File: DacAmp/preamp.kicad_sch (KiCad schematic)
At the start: 34 parts, among them U3 NE5532, U6 NE5532, U7 NE5532, U8 NE5532

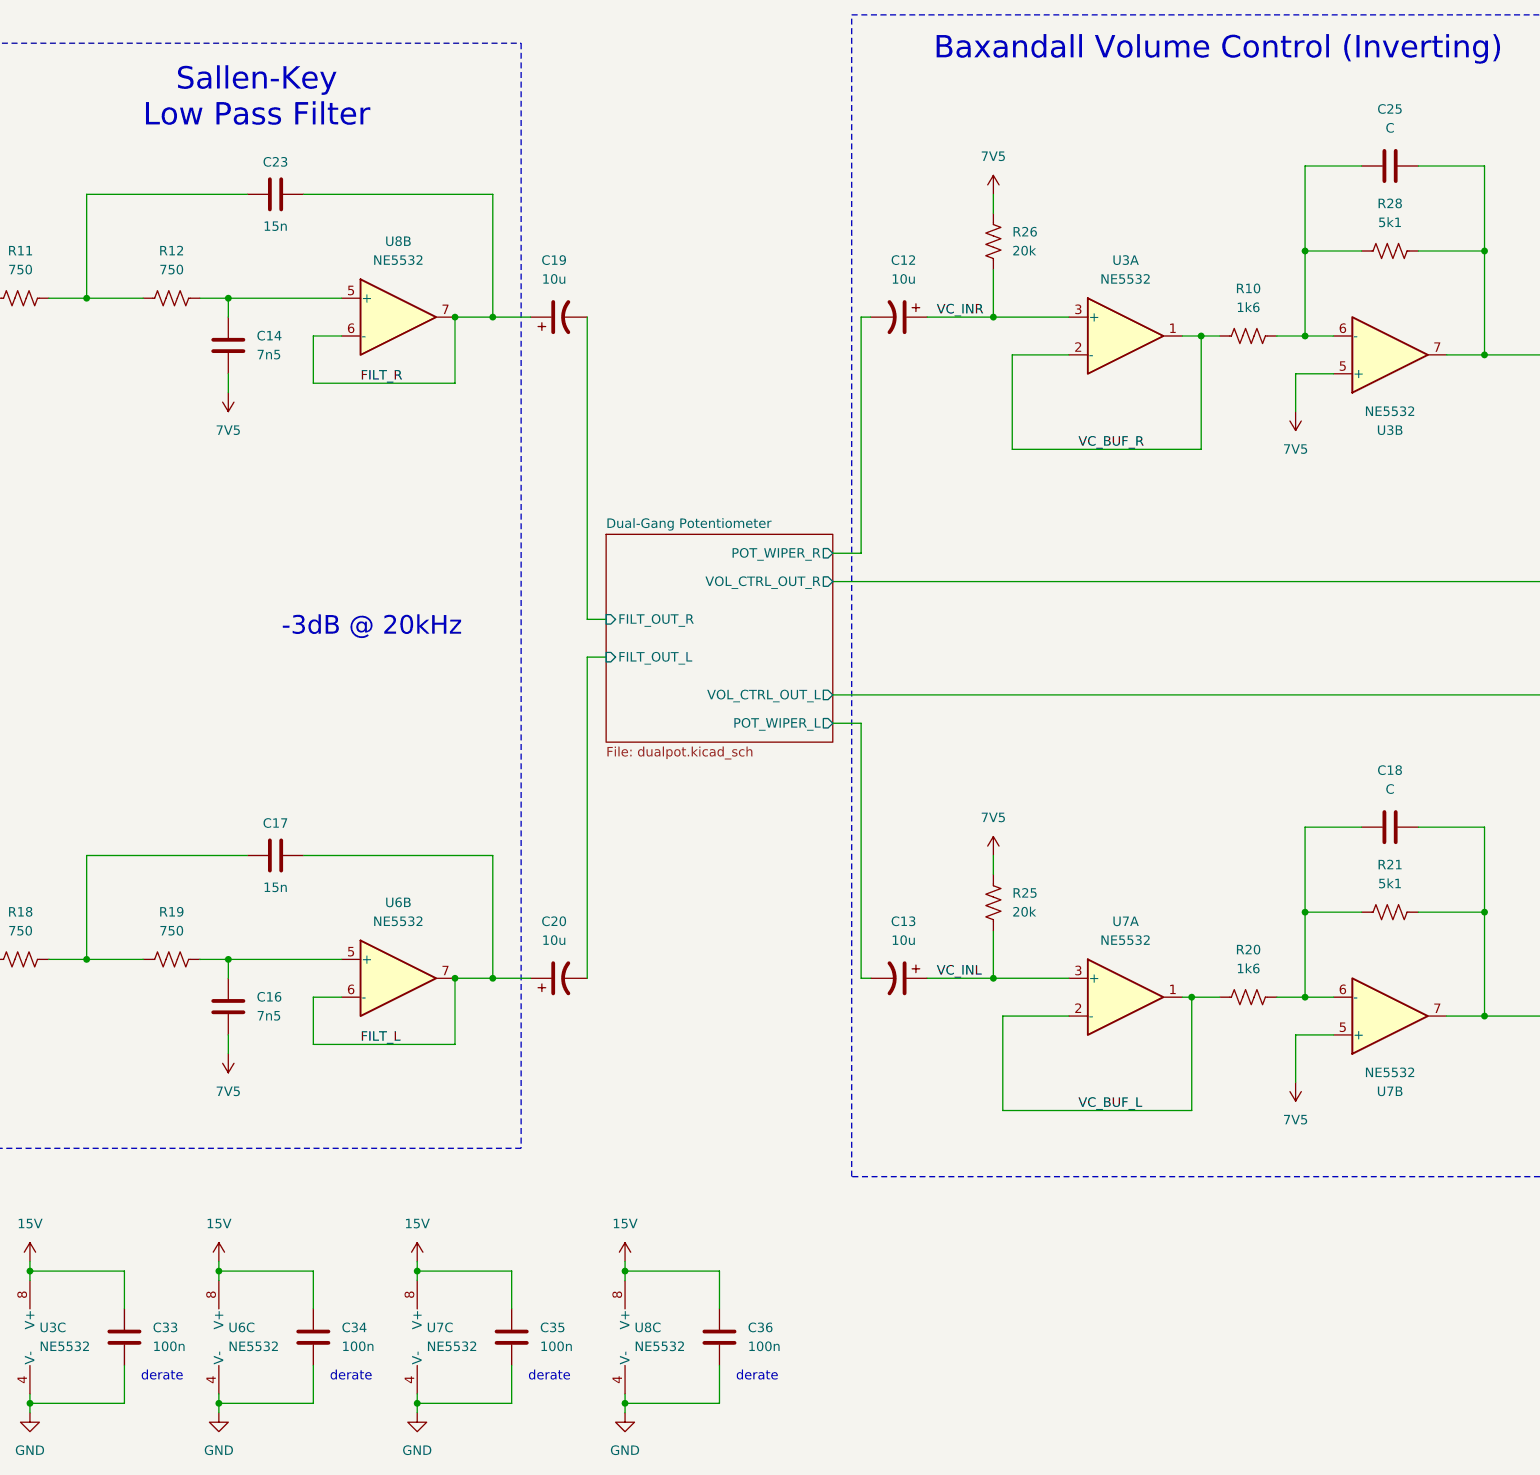
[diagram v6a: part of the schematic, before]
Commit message: add components and footprints
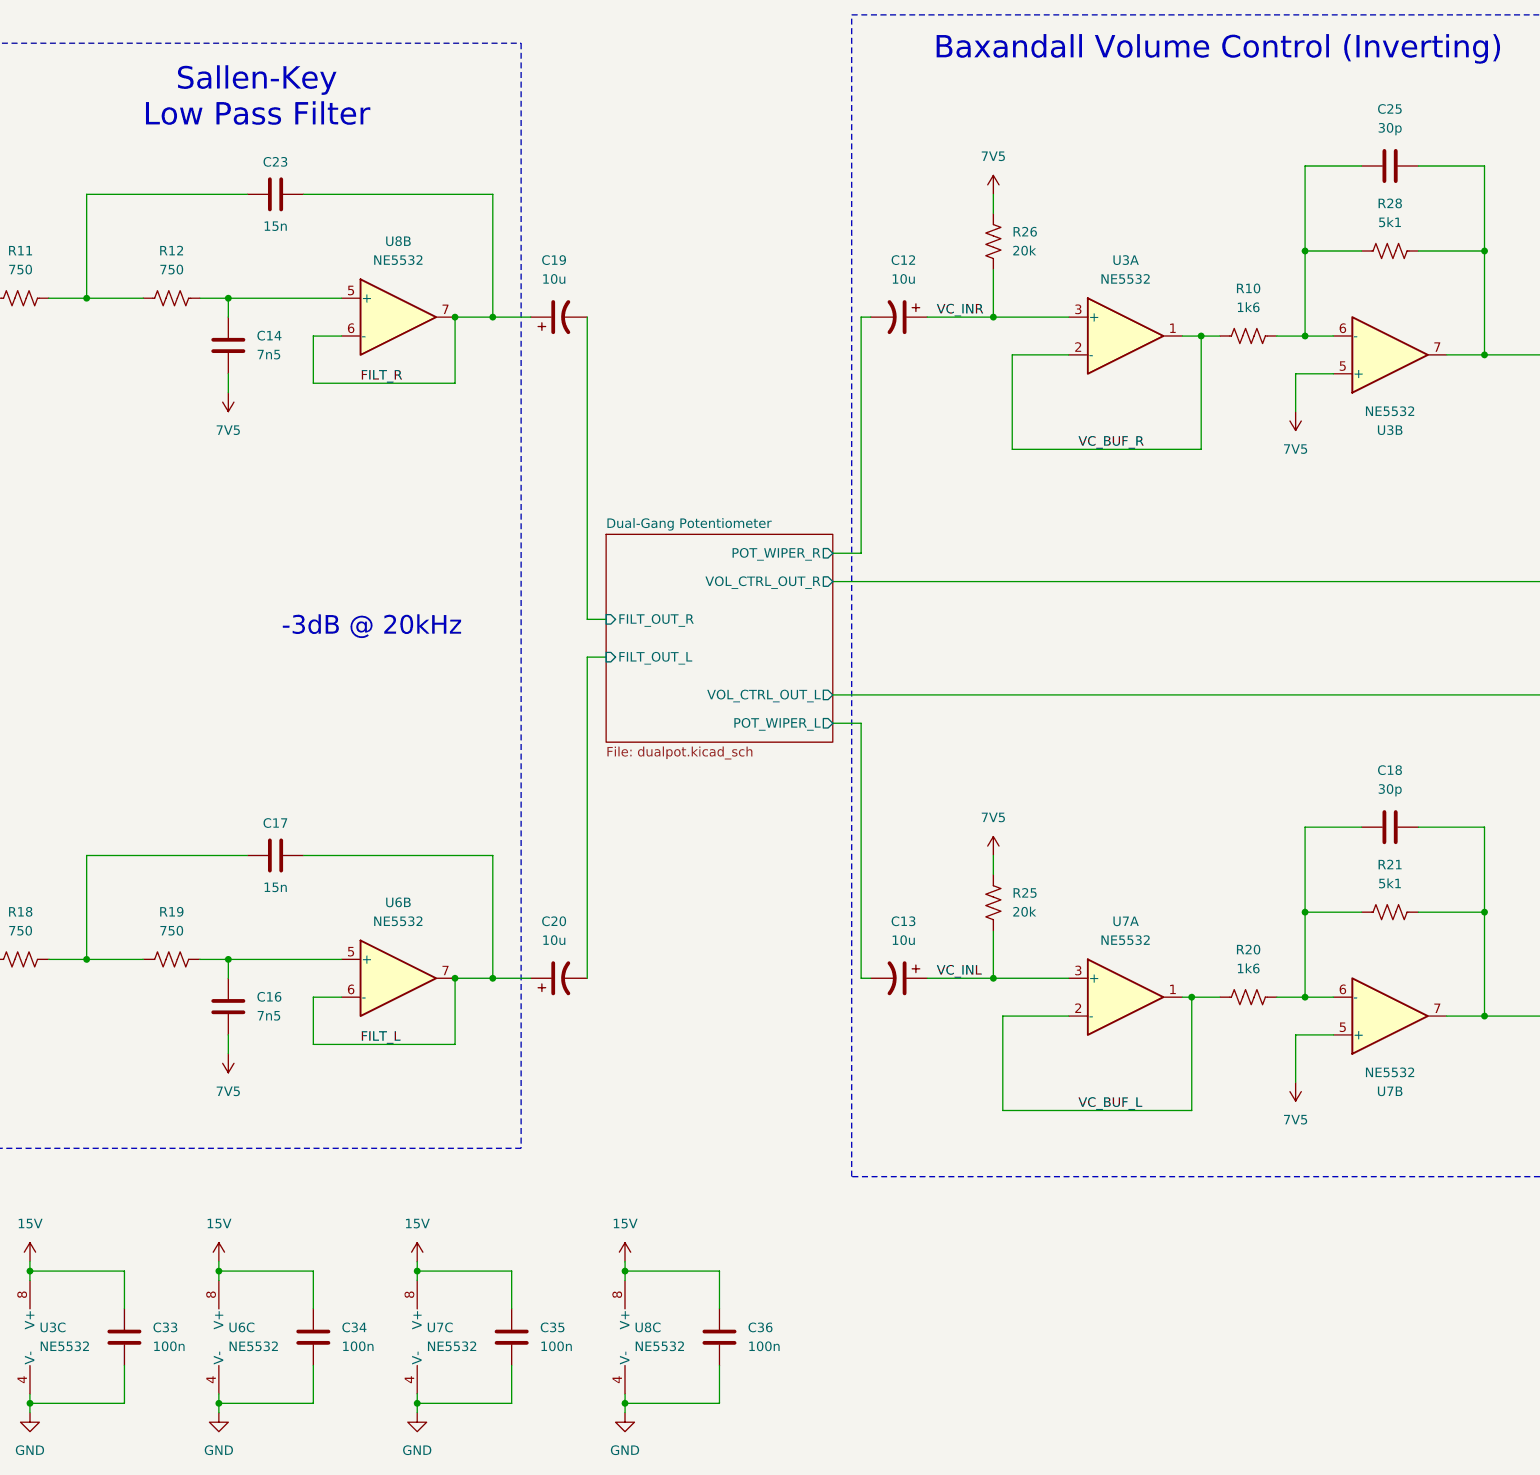
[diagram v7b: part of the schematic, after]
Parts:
- C18, C25: value C -> 30p; footprint (none) -> Capacitor_SMD:C_0402_1005Metric_Pad0.74x0.62mm_HandSolder
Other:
- note removed: "derate"
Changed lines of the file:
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@@
 		)
 	)
-	(text "derate"
-		(exclude_from_sim no)
-		(at 142.24 203.454 0)
-		(effects
-			(font
-				(size 1.27 1.27)
-			)
-		)
-	)
-	(text "derate"
-		(exclude_from_sim no)
-		(at 116.84 203.454 0)
-		(effects
-			(font
-				(size 1.27 1.27)
-			)
-		)
-	)
-	(text "derate"
-		(exclude_from_sim no)
-		(at 196.85 203.454 0)
-		(effects
-			(font
-				(size 1.27 1.27)
-			)
-		)
-	)
 	(text "-3dB @ 20kHz"
 		(exclude_from_sim no)
@@
 		)
 	)
-	(text "derate"
-		(exclude_from_sim no)
-		(at 168.91 203.454 0)
-		(effects
-			(font
-				(size 1.27 1.27)
-			)
-		)
-	)
 	(text "Sallen-Key\nLow Pass Filter"
 		(exclude_from_sim no)
@@
 			)
 		)
-		(property "Value" "C"
+		(property "Value" "30p"
 			(at 281.94 124.46 90)
 			(effects
@@
 			)
 		)
-		(property "Footprint" ""
+		(property "Footprint" "Capacitor_SMD:C_0402_1005Metric_Pad0.74x0.62mm_HandSolder"
 			(at 285.75 128.5748 0)
 			(effects
@@
 			)
 		)
-		(property "Value" "C"
+		(property "Value" "30p"
 			(at 281.94 35.56 90)
 			(effects
@@
 			)
 		)
-		(property "Footprint" ""
+		(property "Footprint" "Capacitor_SMD:C_0402_1005Metric_Pad0.74x0.62mm_HandSolder"
 			(at 285.75 39.6748 0)
 			(effects

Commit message: get ready for layout
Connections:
- net 7V5: no longer C14.2, C16.2, U3.5 (+), U6.3 (+), U7.5 (+), U8.3 (+)
- new net 7V5_L: C16.2, U6.3 (+), U7.5 (+)
- new net 7V5_R: C14.2, U3.5 (+), U8.3 (+)
